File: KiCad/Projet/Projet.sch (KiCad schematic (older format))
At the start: 9 parts, among them P1 Power, P2 Analog, P3 Digital, P4 Digital, P5 CONN_01X01, P6 CONN_01X01, P7 CONN_01X01, P8 CONN_01X01

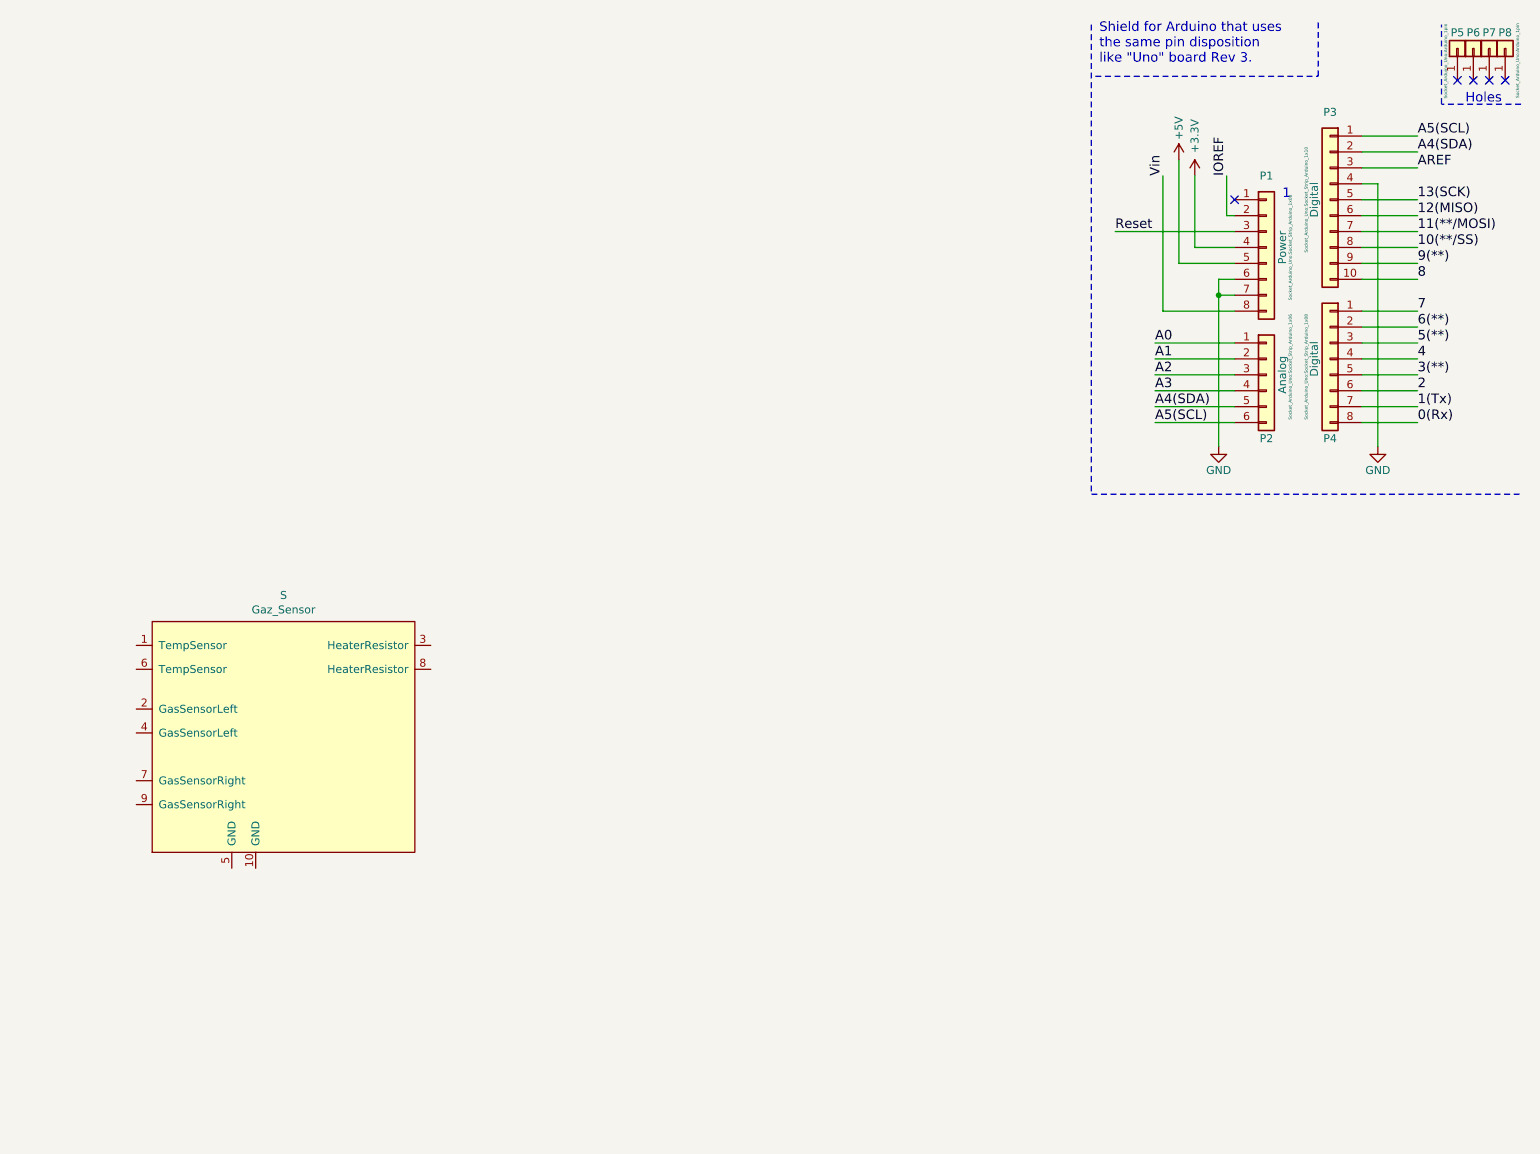
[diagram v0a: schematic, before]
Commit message: Ajouts dans le .sch + Implémentation du symbole du LTC1050
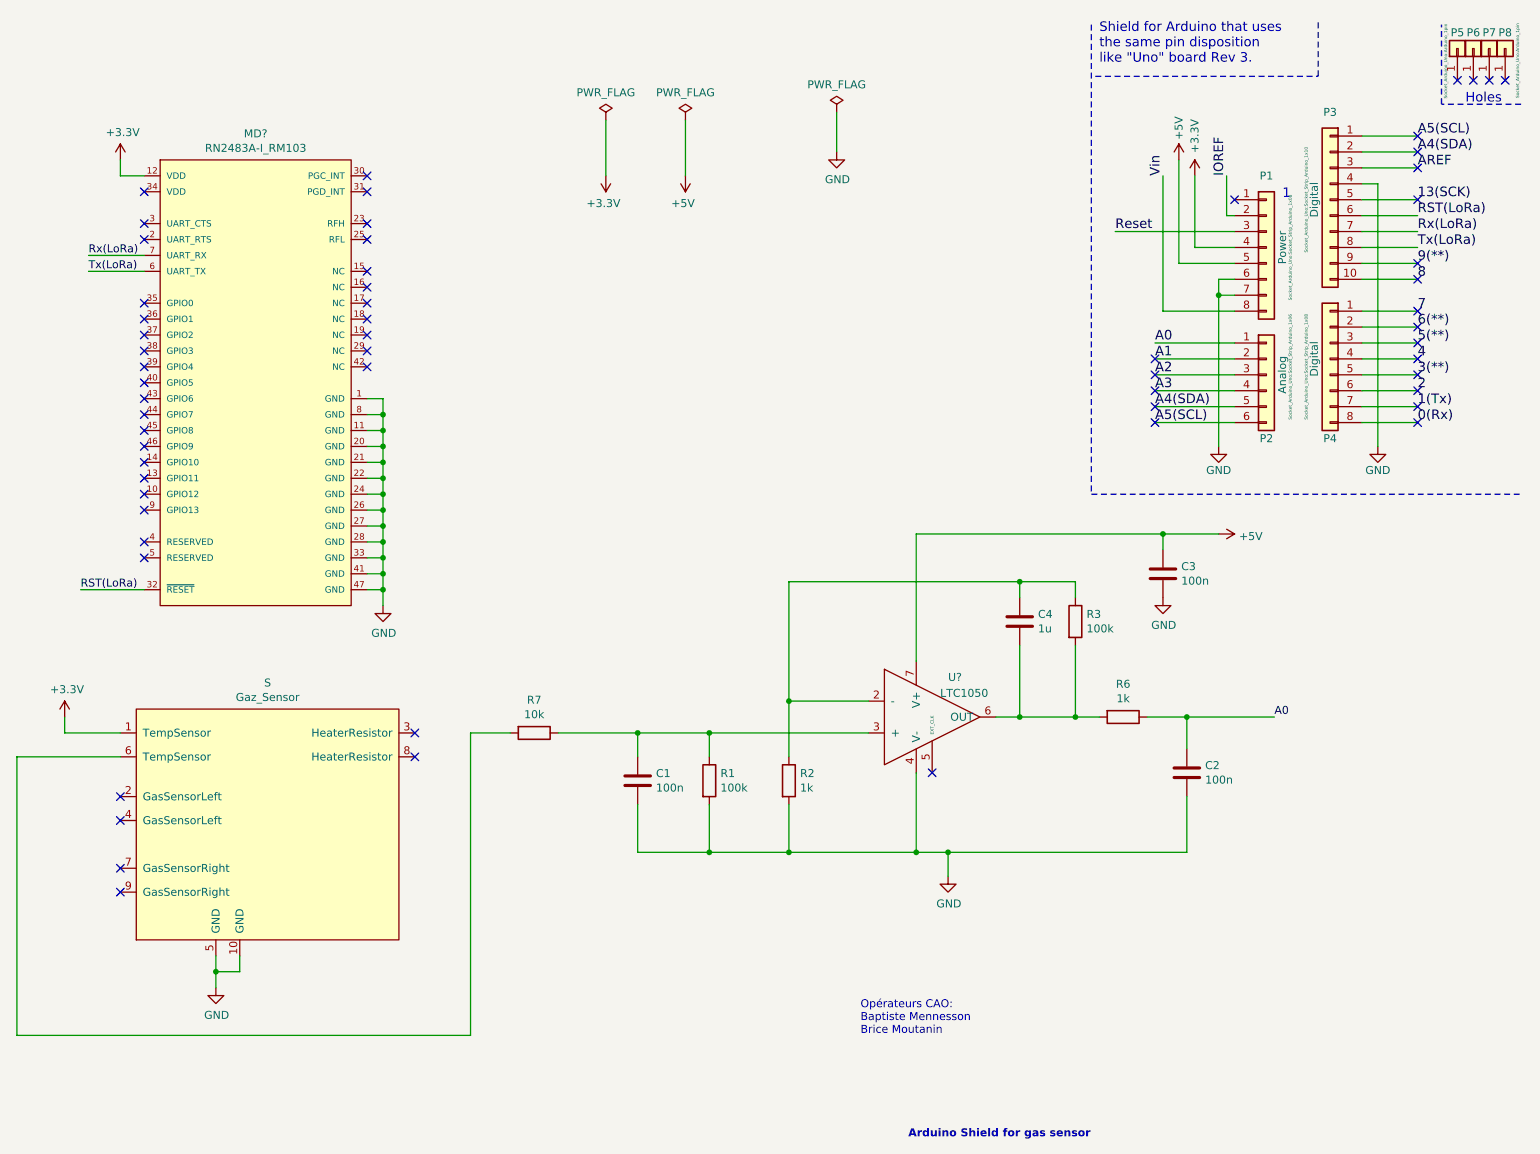
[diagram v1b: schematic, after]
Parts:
- added C1, C2, C3: 100n, symbol Device:C
- added C4: 1u, symbol Device:C
- added MD?: RN2483A-I_RM103, Microchip-RN2483A-I_RM103-0-0-*, symbol Lib_MyProject:RN2483A-I_RM103
- added R1, R3: 100k, symbol Device:R
- added R2, R6: 1k, symbol Device:R
- added R7: 10k, symbol Device:R
- added U?: LTC1050, symbol Lib_MyProject:LTC1050
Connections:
- net +3V3: now also S.1 (TempSensor), MD?.12 (VDD)
- net +5V: now also C3.1, U?.7 (V+)
- net A0: now also C2.1, R6.1
- net GND: now also S.10 (GND), S.5 (GND), C1.2, C2.2, C3.2, MD?.1 (GND), MD?.11 (GND), MD?.20 (GND), MD?.21 (GND), MD?.22 (GND), MD?.24 (GND), MD?.26 (GND), MD?.27 (GND), MD?.28 (GND), MD?.33 (GND), MD?.41 (GND), MD?.47 (GND), MD?.8 (GND), R1.2, R2.2, U?.4 (V-)
- net at S.6 (TempSensor): now also R7.2
- net 10(**/SS) renamed Tx(LoRa)
- net Tx(LoRa): now also MD?.6 (UART_TX)
- net 11(**/MOSI) renamed Rx(LoRa)
- net Rx(LoRa): now also MD?.7 (UART_RX)
- net 12(MISO) renamed RST(LoRa)
- net RST(LoRa): now also MD?.32 (~RESET~)
- new net: C4.1, R2.1, R3.1, U?.2 (-)
- new net: C1.1, R1.1, R7.1, U?.3 (+)
- new net: C4.2, R3.2, R6.2, U?.6 (OUT)
- no-connect marks 5 -> 61
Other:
- note added: "Arduino Shield for gas sensor\n"
- note added: "Opérateurs CAO:\nBaptiste Mennesson\nBrice Moutanin\n"
- moved on the sheet: S

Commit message: Ajouts Empreintes Composants
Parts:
- C1, C2, C3, C4: footprint (none) -> Capacitor_THT:CP_Radial_Tantal_D5.5mm_P5.00mm
- R1, R2, R3, R6, R7: footprint (none) -> Resistor_THT:R_Axial_DIN0207_L6.3mm_D2.5mm_P10.16mm_Horizontal
- S: footprint (none) -> Empreintes_Capteur_Gaz:Empreinte_Capteur_Gaz
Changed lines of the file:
@@
 F 0 "S" H 3325 4665 50  0000 C CNN
 F 1 "Gaz_Sensor" H 3325 4574 50  0000 C CNN
-F 2 "" H 3500 4700 50  0001 C CNN
+F 2 "Empreintes_Capteur_Gaz:Empreinte_Capteur_Gaz" H 3500 4700 50  0001 C CNN
 F 3 "" H 3500 4700 50  0001 C CNN
 	1    3350 4650
@@
 F 0 "C1" H 5765 5296 50  0000 L CNN
 F 1 "100n" H 5765 5205 50  0000 L CNN
-F 2 "" H 5688 5100 50  0001 C CNN
+F 2 "Capacitor_THT:CP_Radial_Tantal_D5.5mm_P5.00mm" H 5688 5100 50  0001 C CNN
 F 3 "~" H 5650 5250 50  0001 C CNN
 	1    5650 5250
@@
 F 0 "R1" H 6170 5296 50  0000 L CNN
 F 1 "100k" H 6170 5205 50  0000 L CNN
-F 2 "" V 6030 5250 50  0001 C CNN
+F 2 "Resistor_THT:R_Axial_DIN0207_L6.3mm_D2.5mm_P10.16mm_Horizontal" V 6030 5250 50  0001 C CNN
 F 3 "~" H 6100 5250 50  0001 C CNN
 	1    6100 5250
@@
 F 0 "R2" H 6670 5296 50  0000 L CNN
 F 1 "1k" H 6670 5205 50  0000 L CNN
-F 2 "" V 6530 5250 50  0001 C CNN
+F 2 "Resistor_THT:R_Axial_DIN0207_L6.3mm_D2.5mm_P10.16mm_Horizontal" V 6530 5250 50  0001 C CNN
 F 3 "~" H 6600 5250 50  0001 C CNN
 	1    6600 5250
@@
 F 0 "R3" H 8470 4296 50  0000 L CNN
 F 1 "100k" H 8470 4205 50  0000 L CNN
-F 2 "" V 8330 4250 50  0001 C CNN
+F 2 "Resistor_THT:R_Axial_DIN0207_L6.3mm_D2.5mm_P10.16mm_Horizontal" V 8330 4250 50  0001 C CNN
 F 3 "~" H 8400 4250 50  0001 C CNN
 	1    8400 4250
@@
 F 0 "C4" H 8165 4296 50  0000 L CNN
 F 1 "1u" H 8165 4205 50  0000 L CNN
-F 2 "" H 8088 4100 50  0001 C CNN
+F 2 "Capacitor_THT:CP_Radial_Tantal_D5.5mm_P5.00mm" H 8088 4100 50  0001 C CNN
 F 3 "~" H 8050 4250 50  0001 C CNN
 	1    8050 4250
@@
 F 0 "R6" V 8493 4850 50  0000 C CNN
 F 1 "1k" V 8584 4850 50  0000 C CNN
-F 2 "" V 8630 4850 50  0001 C CNN
+F 2 "Resistor_THT:R_Axial_DIN0207_L6.3mm_D2.5mm_P10.16mm_Horizontal" V 8630 4850 50  0001 C CNN
 F 3 "~" H 8700 4850 50  0001 C CNN
 	1    8700 4850
@@
 F 0 "C2" H 9215 5246 50  0000 L CNN
 F 1 "100n" H 9215 5155 50  0000 L CNN
-F 2 "" H 9138 5050 50  0001 C CNN
+F 2 "Capacitor_THT:CP_Radial_Tantal_D5.5mm_P5.00mm" H 9138 5050 50  0001 C CNN
 F 3 "~" H 9100 5200 50  0001 C CNN
 	1    9100 5200
@@
 F 0 "C3" H 9065 3996 50  0000 L CNN
 F 1 "100n" H 9065 3905 50  0000 L CNN
-F 2 "" H 8988 3800 50  0001 C CNN
+F 2 "Capacitor_THT:CP_Radial_Tantal_D5.5mm_P5.00mm" H 8988 3800 50  0001 C CNN
 F 3 "~" H 8950 3950 50  0001 C CNN
 	1    8950 3950
@@
 F 0 "R7" V 4793 4950 50  0000 C CNN
 F 1 "10k" V 4884 4950 50  0000 C CNN
-F 2 "" V 4930 4950 50  0001 C CNN
+F 2 "Resistor_THT:R_Axial_DIN0207_L6.3mm_D2.5mm_P10.16mm_Horizontal" V 4930 4950 50  0001 C CNN
 F 3 "~" H 5000 4950 50  0001 C CNN
 	1    5000 4950

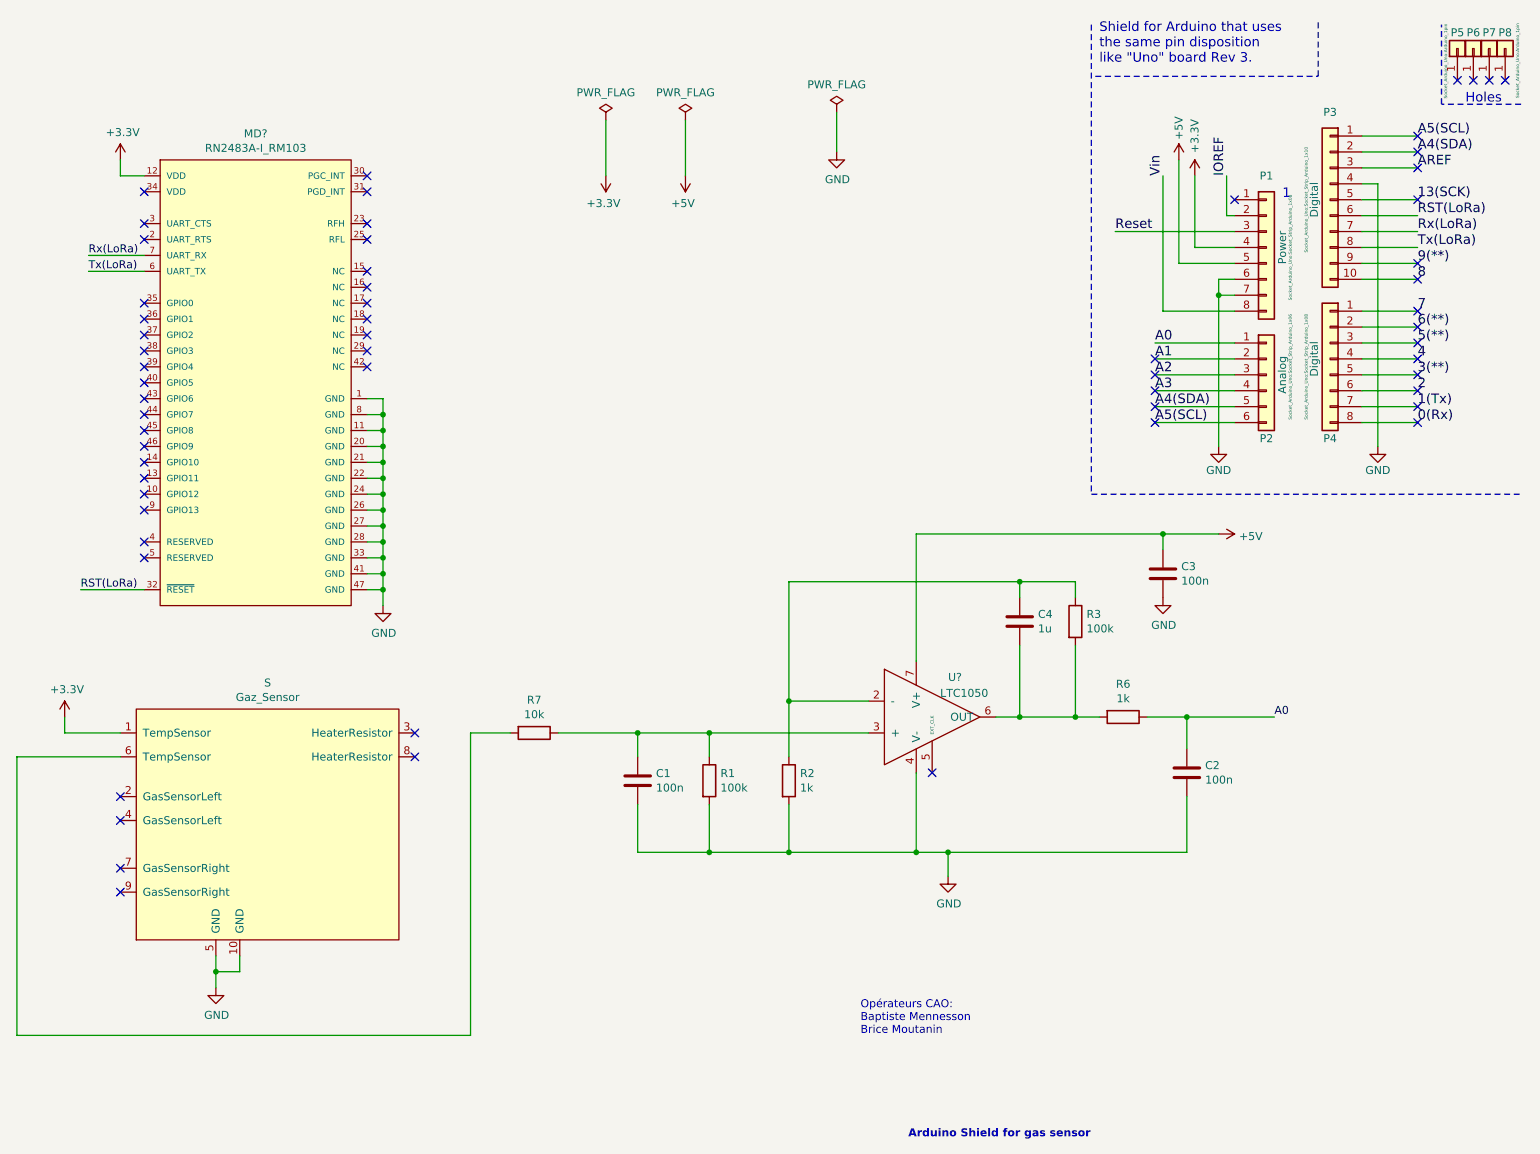
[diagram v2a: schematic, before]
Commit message: Modification sch + Placements pcb
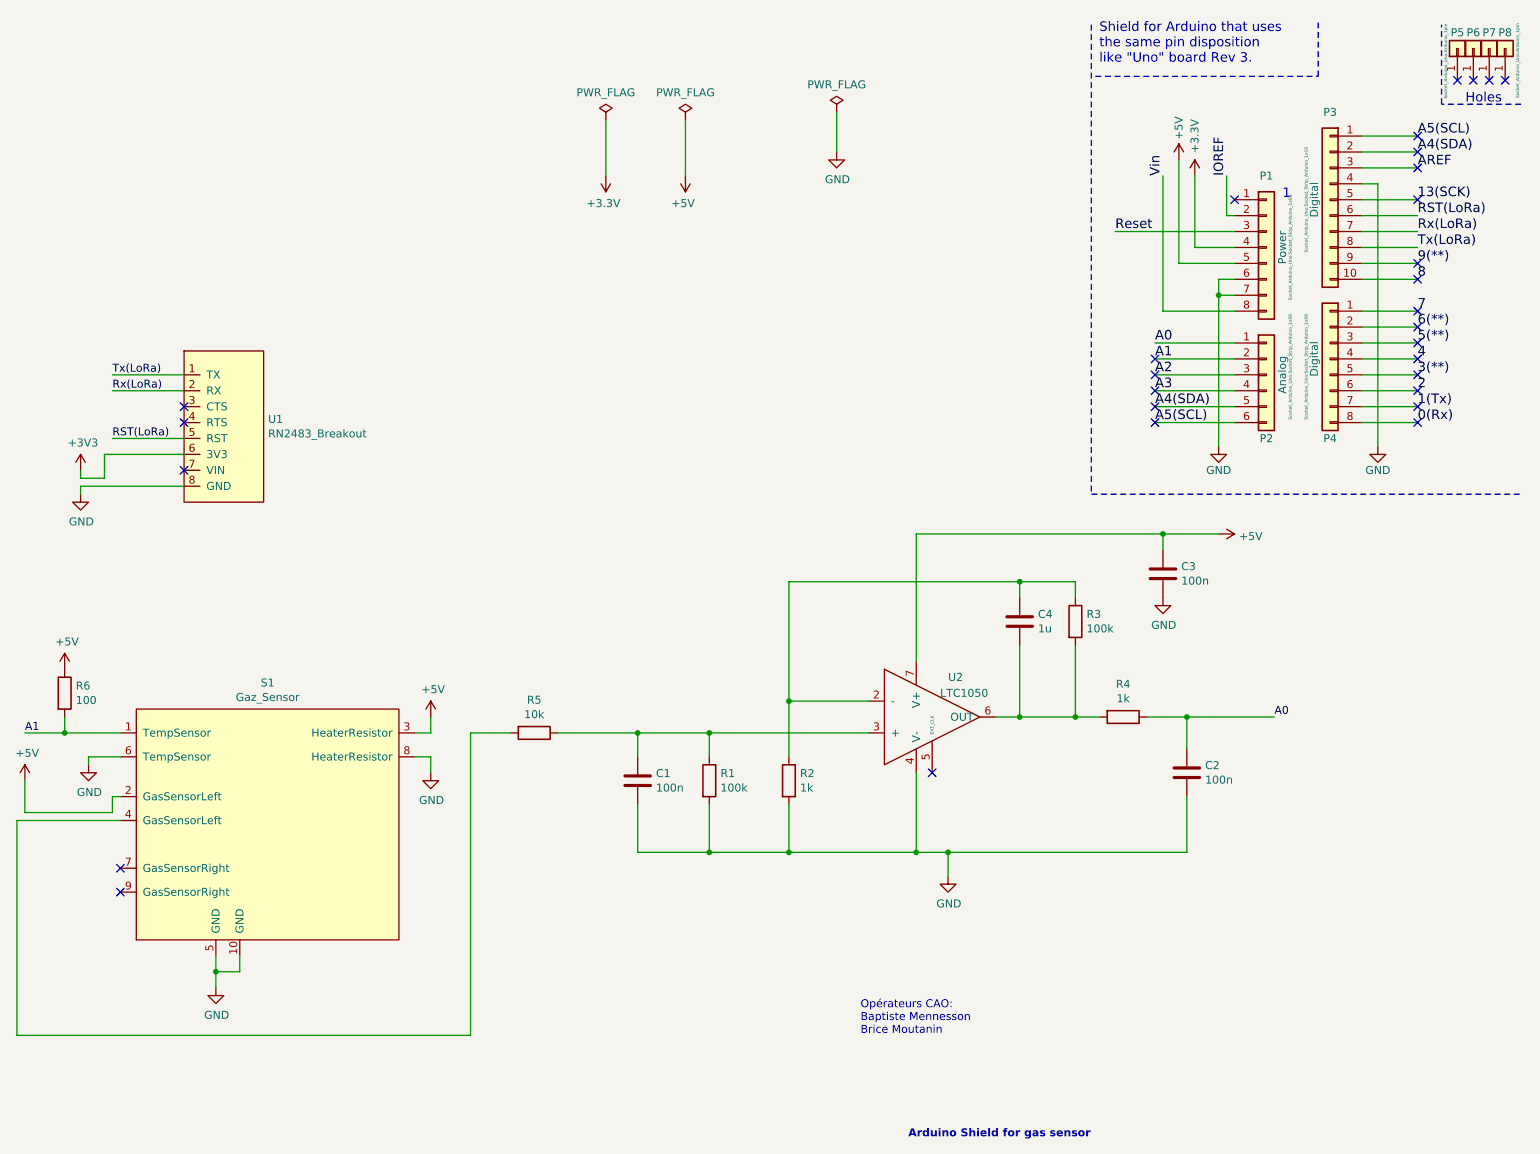
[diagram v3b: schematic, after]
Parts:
- removed MD?: RN2483A-I_RM103, Microchip-RN2483A-I_RM103-0-0-*, symbol Lib_MyProject:RN2483A-I_RM103
- added R6: 100, Resistor_THT:R_Axial_DIN0207_L6.3mm_D2.5mm_P10.16mm_Horizontal, symbol Device:R
- added U1: RN2483_Breakout, Empreinte_RN2483:RN2483_breakout, symbol Lib_MyProject:RN2483_Breakout
- S1: renamed from S; footprint Empreintes_Capteur_Gaz:Empreinte_Capteur_Gaz -> Empreinte_Capteur_Gaz:Empreinte_Capteur_Gaz
- U2: renamed from U?; footprint (none) -> Empreinte_LTC1050:Package_DIP-8_W7.62mm_LongPads
- renumbered R6 to R4, R7 to R5
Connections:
- net +3V3: now also U1.6 (3V3); no longer S1.1 (TempSensor)
- net +5V: now also S1.2 (GasSensorLeft), S1.3 (HeaterResistor), R6.1
- net A1: now also S1.1 (TempSensor), R6.2
- net GND: now also S1.6 (TempSensor), S1.8 (HeaterResistor), U1.8 (GND)
- net RST(LoRa): now also U1.5 (RST)
- net Rx(LoRa): now also U1.2 (RX)
- net Tx(LoRa): now also U1.1 (TX)
- net at S1.4 (GasSensorLeft): now also R5.2
- no-connect marks 61 -> 30

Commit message: V1 PCB + readme
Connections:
- net A0: now also R6.2, S1.1 (TempSensor); no longer C2.1, R4.1
- net A1: now also C2.1, R4.1; no longer R6.2, S1.1 (TempSensor)
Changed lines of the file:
@@
 $EndComp
 Text Label 9650 4850 0    50   ~ 0
-A0
+A1
 Wire Wire Line
 	9100 4850 9650 4850
@@
 	1800 5250 1800 5450
 Text Label 1800 4950 0    50   ~ 0
-A1
+A0
 Wire Wire Line
 	2050 4950 1800 4950
